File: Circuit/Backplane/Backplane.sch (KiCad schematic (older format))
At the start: 50 parts

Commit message: fix pwrclt_pol ,pwrclt and ganged
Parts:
- added R? (x2): 4.7K, symbol R
- added R? (x4): 4.7k, symbol R
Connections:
- net +3V3: now also R?.1
- net GND: now also R?.1, R?.1, R?.1, R?.1, R?.2; no longer R?.2
- net at U?.1 (PWRCTL3/BATEN3): now also R?.2
- net at U?.10 (GANGED/SMBA2/HS_UP): now also R?.1
- net at U?.3 (PWRCTL2/BATEN2): now also R?.2
- net at U?.4 (PWRCTL1/BATEN1): now also R?.2
- net at U?.64 (PWRCTL4/BATEN4): now also R?.2
- net at U?.8 (FULLPWRMGMTz/SMBA1): now also R?.2; no longer R?.2
- net at U?.9 (PWRCTL_POL): now also R?.2
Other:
- moved on the sheet: R?
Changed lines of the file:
@@
 L R R?
 U 1 1 5A5644F5
-P 1800 6050
-F 0 "R?" V 1880 6050 50  0000 C CNN
-F 1 "4.7K" V 1800 6050 50  0000 C CNN
-F 2 "" V 1730 6050 50  0001 C CNN
-F 3 "" H 1800 6050 50  0001 C CNN
-	1    1800 6050
+P 1750 6050
+F 0 "R?" V 1830 6050 50  0000 C CNN
+F 1 "4.7K" V 1750 6050 50  0000 C CNN
+F 2 "" V 1680 6050 50  0001 C CNN
+F 3 "" H 1750 6050 50  0001 C CNN
+	1    1750 6050
 	0    -1   -1   0
 $EndComp
@@
 L +3.3V #PWR?
 U 1 1 5A60DFC7
-P 1650 6050
-F 0 "#PWR?" H 1650 5900 50  0001 C CNN
-F 1 "+3.3V" H 1650 6190 50  0000 C CNN
-F 2 "" H 1650 6050 50  0001 C CNN
-F 3 "" H 1650 6050 50  0001 C CNN
-	1    1650 6050
+P 1600 6050
+F 0 "#PWR?" H 1600 5900 50  0001 C CNN
+F 1 "+3.3V" H 1600 6190 50  0000 C CNN
+F 2 "" H 1600 6050 50  0001 C CNN
+F 3 "" H 1600 6050 50  0001 C CNN
+	1    1600 6050
 	1    0    0    -1
 $EndComp
@@
 L R R?
 U 1 1 5A6127D1
-P 1800 5750
-F 0 "R?" V 1880 5750 50  0000 C CNN
-F 1 "4.7K" V 1800 5750 50  0000 C CNN
-F 2 "" V 1730 5750 50  0001 C CNN
-F 3 "" H 1800 5750 50  0001 C CNN
-	1    1800 5750
+P 1750 5850
+F 0 "R?" V 1830 5850 50  0000 C CNN
+F 1 "4.7K" V 1750 5850 50  0000 C CNN
+F 2 "" V 1680 5850 50  0001 C CNN
+F 3 "" H 1750 5850 50  0001 C CNN
+	1    1750 5850
 	0    -1   -1   0
 $EndComp
@@
 L +3.3V #PWR?
 U 1 1 5A614A5C
-P 1650 5750
-F 0 "#PWR?" H 1650 5600 50  0001 C CNN
-F 1 "+3.3V" H 1650 5890 50  0000 C CNN
-F 2 "" H 1650 5750 50  0001 C CNN
-F 3 "" H 1650 5750 50  0001 C CNN
-	1    1650 5750
+P 1600 5850
+F 0 "#PWR?" H 1600 5700 50  0001 C CNN
+F 1 "+3.3V" H 1600 5990 50  0000 C CNN
+F 2 "" H 1600 5850 50  0001 C CNN
+F 3 "" H 1600 5850 50  0001 C CNN
+	1    1600 5850
 	1    0    0    -1
 $EndComp
@@
 	1    0    0    -1
 $EndComp
+$Comp
+L +5V #PWR?
+U 1 1 5A612588
+P 8950 4100
+F 0 "#PWR?" H 8950 3950 50  0001 C CNN
+F 1 "+5V" H 8950 4240 50  0000 C CNN
+F 2 "" H 8950 4100 50  0001 C CNN
+F 3 "" H 8950 4100 50  0001 C CNN
+	1    8950 4100
+	1    0    0    -1
+$EndComp
+$Comp
+L +3.3V #PWR?
+U 1 1 5A61F59E
+P 750 6000
+F 0 "#PWR?" H 750 5850 50  0001 C CNN
+F 1 "+3.3V" H 750 6140 50  0000 C CNN
+F 2 "" H 750 6000 50  0001 C CNN
+F 3 "" H 750 6000 50  0001 C CNN
+	1    750  6000
+	1    0    0    -1
+$EndComp
+$Comp
+L R R?
+U 1 1 5A61F5A4
+P 1750 5550
+F 0 "R?" V 1830 5550 50  0000 C CNN
+F 1 "4.7K" V 1750 5550 50  0000 C CNN
+F 2 "" V 1680 5550 50  0001 C CNN
+F 3 "" H 1750 5550 50  0001 C CNN
+	1    1750 5550
+	0    -1   -1   0
+$EndComp
+$Comp
+L +3.3V #PWR?
+U 1 1 5A61F5AA
+P 1600 5550
+F 0 "#PWR?" H 1600 5400 50  0001 C CNN
+F 1 "+3.3V" H 1600 5690 50  0000 C CNN
+F 2 "" H 1600 5550 50  0001 C CNN
+F 3 "" H 1600 5550 50  0001 C CNN
+	1    1600 5550
+	1    0    0    -1
+$EndComp
 Wire Wire Line
 	6800 5550 7250 5550
@@
 	8450 6200 8450 4450
 Wire Wire Line
-	1950 6050 3100 6050
-Wire Wire Line
-	3100 5750 1950 5750
-Wire Wire Line
 	3100 6250 3000 6250
 Wire Wire Line
-	2700 6250 2700 6550
-Wire Wire Line
-	2700 6550 4400 6550
+	2700 5950 2700 6550
 Connection ~ 3500 6550
 Wire Wire Line
@@
 Wire Wire Line
 	9150 3800 6850 3800
-$Comp
-L +5V #PWR?
-U 1 1 5A612588
-P 8950 4100
-F 0 "#PWR?" H 8950 3950 50  0001 C CNN
-F 1 "+5V" H 8950 4240 50  0000 C CNN
-F 2 "" H 8950 4100 50  0001 C CNN
-F 3 "" H 8950 4100 50  0001 C CNN
-	1    8950 4100
-	1    0    0    -1
-$EndComp
 Wire Wire Line
 	8950 4100 9450 4100
+Connection ~ 2700 6550
+$Comp
+L GND #PWR?
+U 1 1 5A622BF5
+P 6600 3150
+F 0 "#PWR?" H 6600 2900 50  0001 C CNN
+F 1 "GND" H 6600 3000 50  0000 C CNN
+F 2 "" H 6600 3150 50  0001 C CNN
+F 3 "" H 6600 3150 50  0001 C CNN
+	1    6600 3150
+	1    0    0    -1
+$EndComp
+Wire Wire Line
+	6600 3050 6600 3150
+$Comp
+L R R?
+U 1 1 5A622F6E
+P 6200 3050
+F 0 "R?" V 6280 3050 50  0000 C CNN
+F 1 "4.7k" V 6200 3050 50  0000 C CNN
+F 2 "" V 6130 3050 50  0001 C CNN
+F 3 "" H 6200 3050 50  0001 C CNN
+	1    6200 3050
+	0    1    1    0
+$EndComp
+Wire Wire Line
+	5700 3050 6050 3050
+Wire Wire Line
+	6350 3050 6600 3050
+$Comp
+L GND #PWR?
+U 1 1 5A62378C
+P 6600 3650
+F 0 "#PWR?" H 6600 3400 50  0001 C CNN
+F 1 "GND" H 6600 3500 50  0000 C CNN
+F 2 "" H 6600 3650 50  0001 C CNN
+F 3 "" H 6600 3650 50  0001 C CNN
+	1    6600 3650
+	1    0    0    -1
+$EndComp
+Wire Wire Line
+	6600 3550 6600 3650
+$Comp
+L R R?
+U 1 1 5A623793
+P 6200 3550
+F 0 "R?" V 6280 3550 50  0000 C CNN
+F 1 "4.7k" V 6200 3550 50  0000 C CNN
+F 2 "" V 6130 3550 50  0001 C CNN
+F 3 "" H 6200 3550 50  0001 C CNN
+	1    6200 3550
+	0    1    1    0
+$EndComp
+Wire Wire Line
+	5700 3550 6050 3550
+Wire Wire Line
+	6350 3550 6600 3550
+$Comp
+L GND #PWR?
+U 1 1 5A623876
+P 6600 4150
+F 0 "#PWR?" H 6600 3900 50  0001 C CNN
+F 1 "GND" H 6600 4000 50  0000 C CNN
+F 2 "" H 6600 4150 50  0001 C CNN
+F 3 "" H 6600 4150 50  0001 C CNN
+	1    6600 4150
+	1    0    0    -1
+$EndComp
+$Comp
+L R R?
+U 1 1 5A62387C
+P 6200 4050
+F 0 "R?" V 6280 4050 50  0000 C CNN
+F 1 "4.7k" V 6200 4050 50  0000 C CNN
+F 2 "" V 6130 4050 50  0001 C CNN
+F 3 "" H 6200 4050 50  0001 C CNN
+	1    6200 4050
+	0    1    1    0
+$EndComp
+Wire Wire Line
+	5700 4050 6050 4050
+Wire Wire Line
+	6350 4050 6600 4050
+$Comp
+L GND #PWR?
+U 1 1 5A623955
+P 6600 4650
+F 0 "#PWR?" H 6600 4400 50  0001 C CNN
+F 1 "GND" H 6600 4500 50  0000 C CNN
+F 2 "" H 6600 4650 50  0001 C CNN
+F 3 "" H 6600 4650 50  0001 C CNN
+	1    6600 4650
+	1    0    0    -1
+$EndComp
+$Comp
+L R R?
+U 1 1 5A62395B
+P 6200 4550
+F 0 "R?" V 6280 4550 50  0000 C CNN
+F 1 "4.7k" V 6200 4550 50  0000 C CNN
+F 2 "" V 6130 4550 50  0001 C CNN
+F 3 "" H 6200 4550 50  0001 C CNN
+	1    6200 4550
+	0    1    1    0
+$EndComp
+Wire Wire Line
+	5700 4550 6050 4550
+Wire Wire Line
+	6350 4550 6600 4550
+Wire Wire Line
+	6600 4050 6600 4150
+Wire Wire Line
+	6600 4550 6600 4650
+$Comp
+L R R?
+U 1 1 5A6242AD
+P 2850 5950
+F 0 "R?" V 2930 5950 50  0000 C CNN
+F 1 "4.7K" V 2850 5950 50  0000 C CNN
+F 2 "" V 2780 5950 50  0001 C CNN
+F 3 "" H 2850 5950 50  0001 C CNN
+	1    2850 5950
+	0    1    1    0
+$EndComp
+Wire Wire Line
+	2700 6550 4400 6550
+Wire Wire Line
+	3100 5950 3000 5950
+Wire Wire Line
+	3100 6050 1900 6050
+Wire Wire Line
+	3100 5850 1900 5850
+Wire Wire Line
+	3100 5750 1900 5750
+Wire Wire Line
+	1900 5750 1900 5550
 $EndSCHEMATC

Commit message: fix rs232 gnd11
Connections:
- net GND: no longer CON?.A4 (GND), J?.1 (Pin_1)
- new net: CON?.A4 (GND), J?.1 (Pin_1)
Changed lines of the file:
@@
 Wire Wire Line
 	7200 6200 8450 6200
-Connection ~ 8450 6200
 Wire Wire Line
 	7150 3500 8400 3500
@@
 	1400 2450 1600 2450
 Wire Wire Line
-	8450 6200 8450 4450
-Wire Wire Line
 	3100 6250 3000 6250
 Wire Wire Line
@@
 Connection ~ 6550 4850
 Connection ~ 8400 5000
-Connection ~ 8450 4450
 Wire Wire Line
 	8400 4750 9050 4750

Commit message: fix pcie ComBridge
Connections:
- net +5V: now also J?.2 (Pin_2); no longer J?.3 (Pin_3)
- net GND: now also J?.3 (Pin_3); no longer CON?.B7 (GND), J?.1 (Pin_1)
- net at CON?.B6 (SMDAT): now also J?.1 (Pin_1); no longer J?.2 (Pin_2)
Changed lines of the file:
@@
 L +5V #PWR?
 U 1 1 5A612588
-P 8950 4100
-F 0 "#PWR?" H 8950 3950 50  0001 C CNN
-F 1 "+5V" H 8950 4240 50  0000 C CNN
-F 2 "" H 8950 4100 50  0001 C CNN
-F 3 "" H 8950 4100 50  0001 C CNN
-	1    8950 4100
+P 8950 4000
+F 0 "#PWR?" H 8950 3850 50  0001 C CNN
+F 1 "+5V" H 8950 4140 50  0000 C CNN
+F 2 "" H 8950 4000 50  0001 C CNN
+F 3 "" H 8950 4000 50  0001 C CNN
+	1    8950 4000
 	1    0    0    -1
 $EndComp
@@
 	1    0    0    -1
 $EndComp
+$Comp
+L GND #PWR?
+U 1 1 5A622BF5
+P 6600 3150
+F 0 "#PWR?" H 6600 2900 50  0001 C CNN
+F 1 "GND" H 6600 3000 50  0000 C CNN
+F 2 "" H 6600 3150 50  0001 C CNN
+F 3 "" H 6600 3150 50  0001 C CNN
+	1    6600 3150
+	1    0    0    -1
+$EndComp
+$Comp
+L R R?
+U 1 1 5A622F6E
+P 6200 3050
+F 0 "R?" V 6280 3050 50  0000 C CNN
+F 1 "4.7k" V 6200 3050 50  0000 C CNN
+F 2 "" V 6130 3050 50  0001 C CNN
+F 3 "" H 6200 3050 50  0001 C CNN
+	1    6200 3050
+	0    1    1    0
+$EndComp
+$Comp
+L GND #PWR?
+U 1 1 5A62378C
+P 6600 3650
+F 0 "#PWR?" H 6600 3400 50  0001 C CNN
+F 1 "GND" H 6600 3500 50  0000 C CNN
+F 2 "" H 6600 3650 50  0001 C CNN
+F 3 "" H 6600 3650 50  0001 C CNN
+	1    6600 3650
+	1    0    0    -1
+$EndComp
+$Comp
+L R R?
+U 1 1 5A623793
+P 6200 3550
+F 0 "R?" V 6280 3550 50  0000 C CNN
+F 1 "4.7k" V 6200 3550 50  0000 C CNN
+F 2 "" V 6130 3550 50  0001 C CNN
+F 3 "" H 6200 3550 50  0001 C CNN
+	1    6200 3550
+	0    1    1    0
+$EndComp
+$Comp
+L GND #PWR?
+U 1 1 5A623876
+P 6600 4150
+F 0 "#PWR?" H 6600 3900 50  0001 C CNN
+F 1 "GND" H 6600 4000 50  0000 C CNN
+F 2 "" H 6600 4150 50  0001 C CNN
+F 3 "" H 6600 4150 50  0001 C CNN
+	1    6600 4150
+	1    0    0    -1
+$EndComp
+$Comp
+L R R?
+U 1 1 5A62387C
+P 6200 4050
+F 0 "R?" V 6280 4050 50  0000 C CNN
+F 1 "4.7k" V 6200 4050 50  0000 C CNN
+F 2 "" V 6130 4050 50  0001 C CNN
+F 3 "" H 6200 4050 50  0001 C CNN
+	1    6200 4050
+	0    1    1    0
+$EndComp
+$Comp
+L GND #PWR?
+U 1 1 5A623955
+P 6600 4650
+F 0 "#PWR?" H 6600 4400 50  0001 C CNN
+F 1 "GND" H 6600 4500 50  0000 C CNN
+F 2 "" H 6600 4650 50  0001 C CNN
+F 3 "" H 6600 4650 50  0001 C CNN
+	1    6600 4650
+	1    0    0    -1
+$EndComp
+$Comp
+L R R?
+U 1 1 5A62395B
+P 6200 4550
+F 0 "R?" V 6280 4550 50  0000 C CNN
+F 1 "4.7k" V 6200 4550 50  0000 C CNN
+F 2 "" V 6130 4550 50  0001 C CNN
+F 3 "" H 6200 4550 50  0001 C CNN
+	1    6200 4550
+	0    1    1    0
+$EndComp
+$Comp
+L R R?
+U 1 1 5A6242AD
+P 2850 5950
+F 0 "R?" V 2930 5950 50  0000 C CNN
+F 1 "4.7K" V 2850 5950 50  0000 C CNN
+F 2 "" V 2780 5950 50  0001 C CNN
+F 3 "" H 2850 5950 50  0001 C CNN
+	1    2850 5950
+	0    1    1    0
+$EndComp
 Wire Wire Line
 	6800 5550 7250 5550
@@
 	8400 4250 8400 4350
 Wire Wire Line
-	7250 4450 7200 4450
+	7000 4450 7250 4450
 Wire Wire Line
 	7200 4450 7200 6200
 Wire Wire Line
 	7200 5450 7250 5450
-Connection ~ 7200 4750
 Wire Wire Line
 	7200 5750 7250 5750
@@
 	10150 3450 10150 3500
 Wire Wire Line
-	6850 4750 7250 4750
-Wire Wire Line
-	6850 3800 6850 4750
-Wire Wire Line
-	6900 4650 7250 4650
-Wire Wire Line
-	6900 3850 6900 4650
-Wire Wire Line
 	8400 3500 8400 1750
 Wire Wire Line
@@
 	5050 950  5050 1100
 Wire Wire Line
-	9050 4000 9450 4000
-Wire Wire Line
-	9150 3900 9450 3900
-Wire Wire Line
-	6900 3850 9050 3850
-Wire Wire Line
-	9050 3850 9050 4000
-Wire Wire Line
-	9150 3900 9150 3800
-Wire Wire Line
-	9150 3800 6850 3800
-Wire Wire Line
-	8950 4100 9450 4100
+	8950 4000 9450 4000
 Connection ~ 2700 6550
-$Comp
-L GND #PWR?
-U 1 1 5A622BF5
-P 6600 3150
-F 0 "#PWR?" H 6600 2900 50  0001 C CNN
-F 1 "GND" H 6600 3000 50  0000 C CNN
-F 2 "" H 6600 3150 50  0001 C CNN
-F 3 "" H 6600 3150 50  0001 C CNN
-	1    6600 3150
-	1    0    0    -1
-$EndComp
 Wire Wire Line
 	6600 3050 6600 3150
-$Comp
-L R R?
-U 1 1 5A622F6E
-P 6200 3050
-F 0 "R?" V 6280 3050 50  0000 C CNN
-F 1 "4.7k" V 6200 3050 50  0000 C CNN
-F 2 "" V 6130 3050 50  0001 C CNN
-F 3 "" H 6200 3050 50  0001 C CNN
-	1    6200 3050
-	0    1    1    0
-$EndComp
 Wire Wire Line
 	5700 3050 6050 3050
 Wire Wire Line
 	6350 3050 6600 3050
-$Comp
-L GND #PWR?
-U 1 1 5A62378C
-P 6600 3650
-F 0 "#PWR?" H 6600 3400 50  0001 C CNN
-F 1 "GND" H 6600 3500 50  0000 C CNN
-F 2 "" H 6600 3650 50  0001 C CNN
-F 3 "" H 6600 3650 50  0001 C CNN
-	1    6600 3650
-	1    0    0    -1
-$EndComp
 Wire Wire Line
 	6600 3550 6600 3650
-$Comp
-L R R?
-U 1 1 5A623793
-P 6200 3550
-F 0 "R?" V 6280 3550 50  0000 C CNN
-F 1 "4.7k" V 6200 3550 50  0000 C CNN
-F 2 "" V 6130 3550 50  0001 C CNN
-F 3 "" H 6200 3550 50  0001 C CNN
-	1    6200 3550
-	0    1    1    0
-$EndComp
 Wire Wire Line
 	5700 3550 6050 3550
 Wire Wire Line
 	6350 3550 6600 3550
-$Comp
-L GND #PWR?
-U 1 1 5A623876
-P 6600 4150
-F 0 "#PWR?" H 6600 3900 50  0001 C CNN
-F 1 "GND" H 6600 4000 50  0000 C CNN
-F 2 "" H 6600 4150 50  0001 C CNN
-F 3 "" H 6600 4150 50  0001 C CNN
-	1    6600 4150
-	1    0    0    -1
-$EndComp
-$Comp
-L R R?
-U 1 1 5A62387C
-P 6200 4050
-F 0 "R?" V 6280 4050 50  0000 C CNN
-F 1 "4.7k" V 6200 4050 50  0000 C CNN
-F 2 "" V 6130 4050 50  0001 C CNN
-F 3 "" H 6200 4050 50  0001 C CNN
-	1    6200 4050
-	0    1    1    0
-$EndComp
 Wire Wire Line
 	5700 4050 6050 4050
 Wire Wire Line
 	6350 4050 6600 4050
-$Comp
-L GND #PWR?
-U 1 1 5A623955
-P 6600 4650
-F 0 "#PWR?" H 6600 4400 50  0001 C CNN
-F 1 "GND" H 6600 4500 50  0000 C CNN
-F 2 "" H 6600 4650 50  0001 C CNN
-F 3 "" H 6600 4650 50  0001 C CNN
-	1    6600 4650
-	1    0    0    -1
-$EndComp
-$Comp
-L R R?
-U 1 1 5A62395B
-P 6200 4550
-F 0 "R?" V 6280 4550 50  0000 C CNN
-F 1 "4.7k" V 6200 4550 50  0000 C CNN
-F 2 "" V 6130 4550 50  0001 C CNN
-F 3 "" H 6200 4550 50  0001 C CNN
-	1    6200 4550
-	0    1    1    0
-$EndComp
 Wire Wire Line
 	5700 4550 6050 4550
@@
 Wire Wire Line
 	6600 4550 6600 4650
-$Comp
-L R R?
-U 1 1 5A6242AD
-P 2850 5950
-F 0 "R?" V 2930 5950 50  0000 C CNN
-F 1 "4.7K" V 2850 5950 50  0000 C CNN
-F 2 "" V 2780 5950 50  0001 C CNN
-F 3 "" H 2850 5950 50  0001 C CNN
-	1    2850 5950
-	0    1    1    0
-$EndComp
 Wire Wire Line
 	2700 6550 4400 6550
@@
 Wire Wire Line
 	1900 5750 1900 5550
+Wire Wire Line
+	6850 3800 6850 4650
+Wire Wire Line
+	6850 4650 7250 4650
+Wire Wire Line
+	9450 3900 9450 3800
+Wire Wire Line
+	9450 3800 6850 3800
+Wire Wire Line
+	9450 4100 8650 4100
+Wire Wire Line
+	8650 4100 8650 3900
+Wire Wire Line
+	8650 3900 7000 3900
+Wire Wire Line
+	7000 3900 7000 4450
+Connection ~ 7200 4450
 $EndSCHEMATC

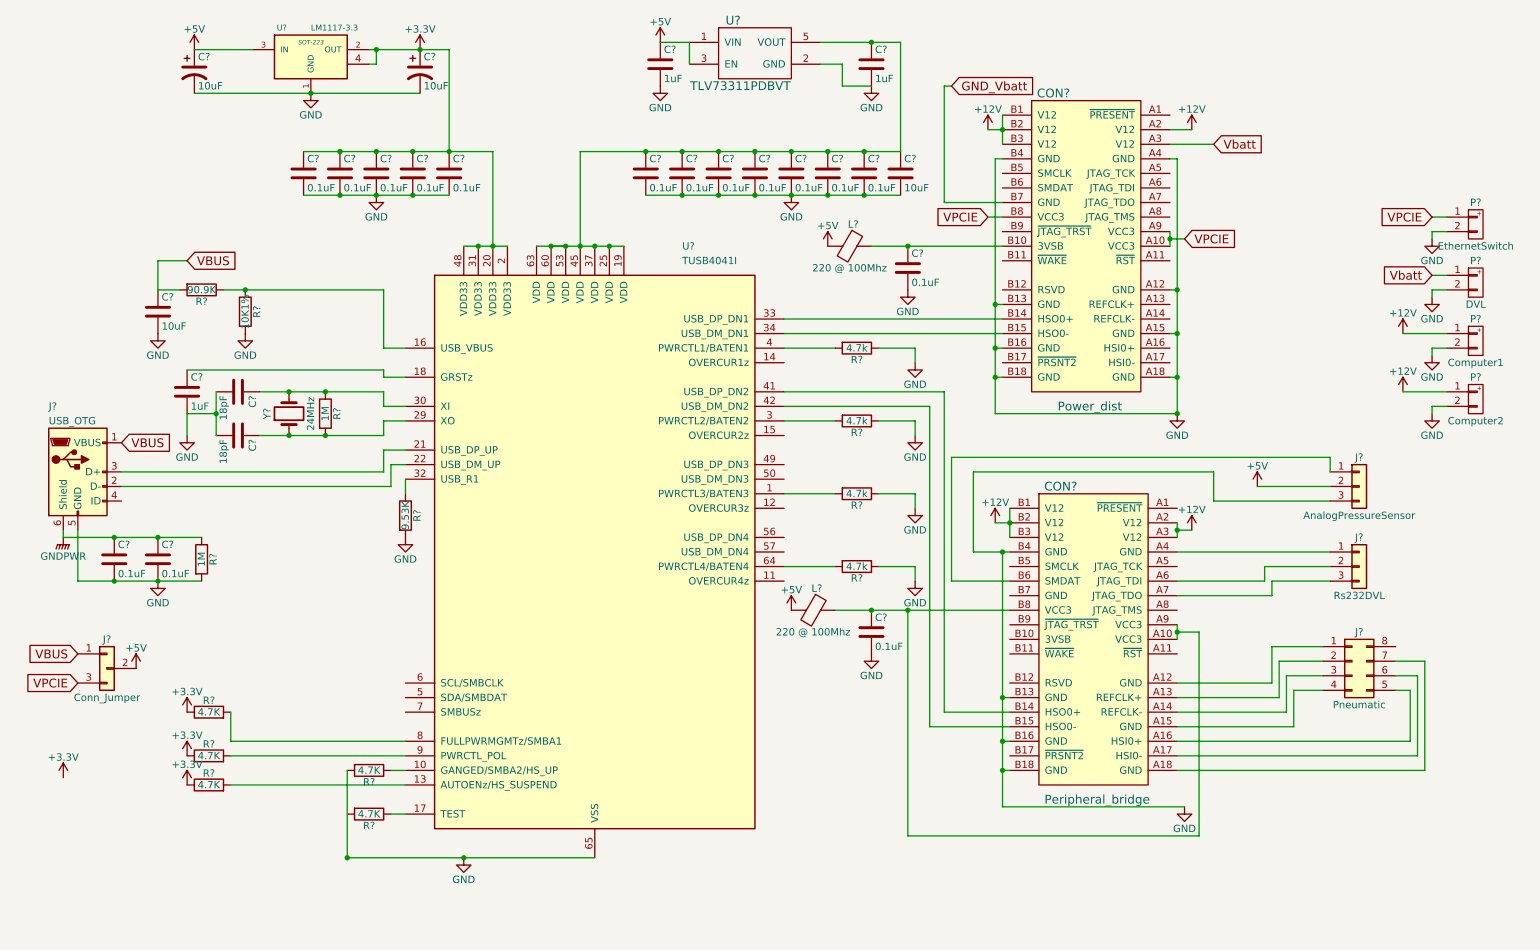
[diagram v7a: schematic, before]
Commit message: add imaging sonar charge vbatt to +batt , gnd to gnda in pwrdist and DVL
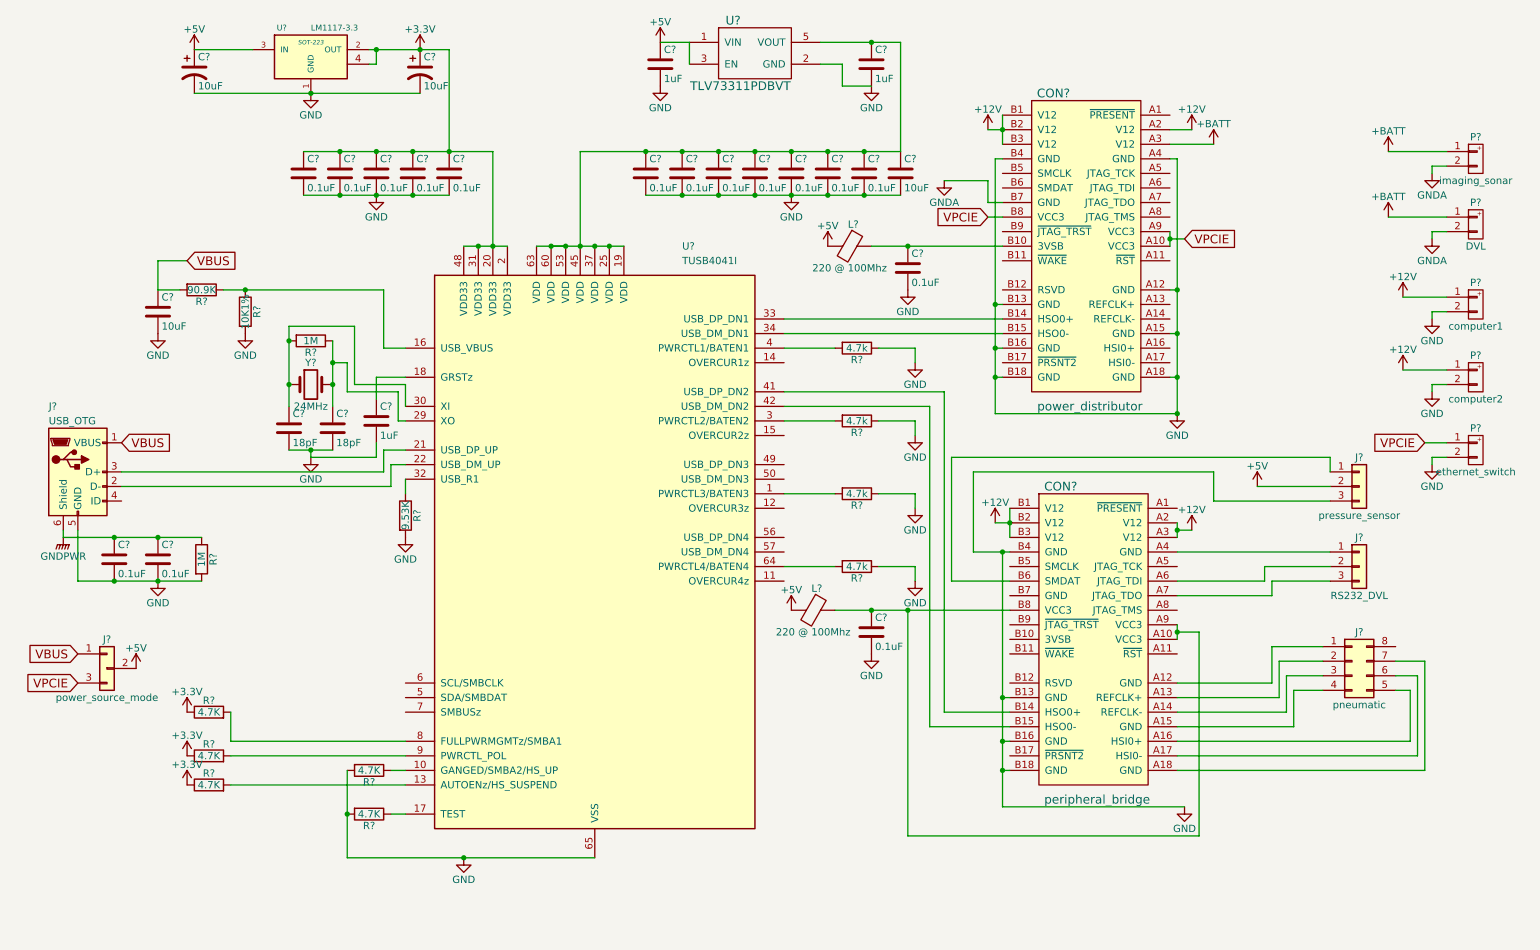
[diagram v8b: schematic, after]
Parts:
- removed C? (x2): 18pF, symbol C
- removed C?: 1uF, symbol C
- removed R?: 1M, symbol R
- removed Y?: 24MHz, symbol Crystal
- added C? (x2): 18pF, symbol C
- added C?: 1uF, symbol C
- added P?: imaging_sonar, symbol XT30
- added R?: 1M, symbol R
- added Y?: 24MHz, symbol Crystal
- CON?: value Power_dist -> power_distributor
- CON?: value Peripheral_bridge -> peripheral_bridge
- J?: value AnalogPressureSensor -> pressure_sensor
- J?: value Rs232DVL -> RS232_DVL
- J?: value Pneumatic -> pneumatic
- J?: value Conn_Jumper -> power_source_mode
- P?: value EthernetSwitch -> ethernet_switch
- P?: value Computer1 -> computer1
- P?: value Computer2 -> computer2
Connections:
- net GND: now also R?.2, C?.2, C?.2, C?.2; no longer P?.2 (P2)
- net at U?.18 (GRSTz): now also C?.1
- net at U?.29 (XO): now also C?.1, R?.1, Y?.2
- net at U?.30 (XI): now also C?.1, R?.2, Y?.1
- net GND_Vbatt renamed GNDA
- net GNDA: now also P?.2 (P2), P?.2 (P2)
- net Vbatt renamed +BATT
- net +BATT: now also P?.1 (P1)
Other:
- moved on the sheet: P?
